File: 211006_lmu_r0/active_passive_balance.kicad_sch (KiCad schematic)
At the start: 37 parts, among them Q11 BSS308PE, T16 BUK9K13-60EX, T4 750312504

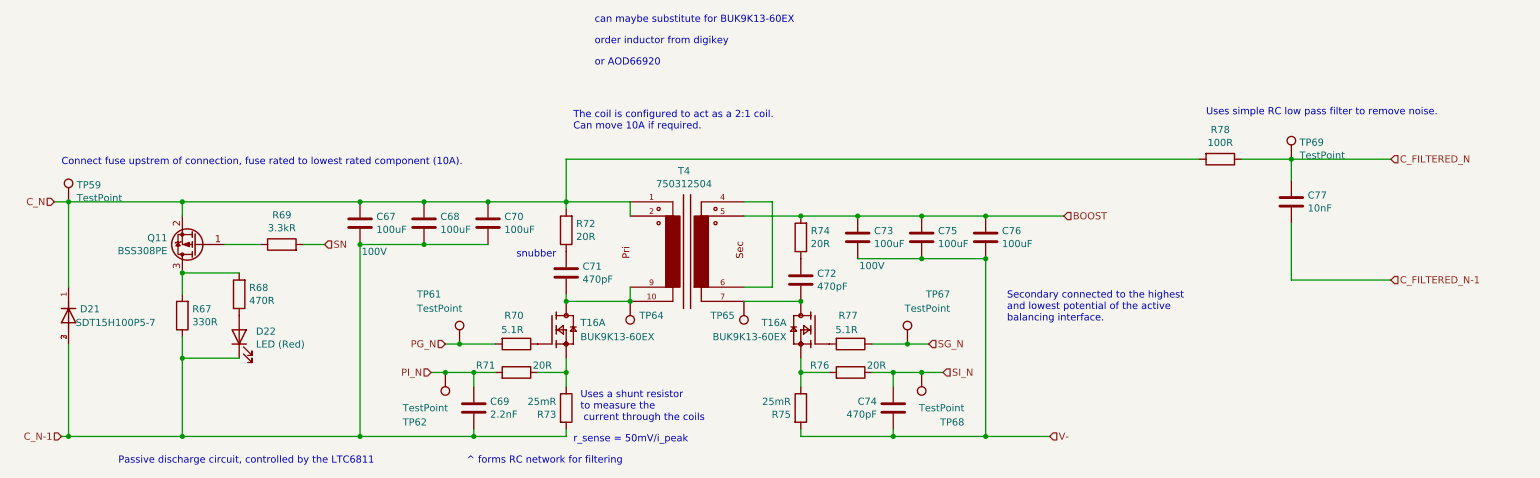
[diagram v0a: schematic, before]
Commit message: moved micro into position
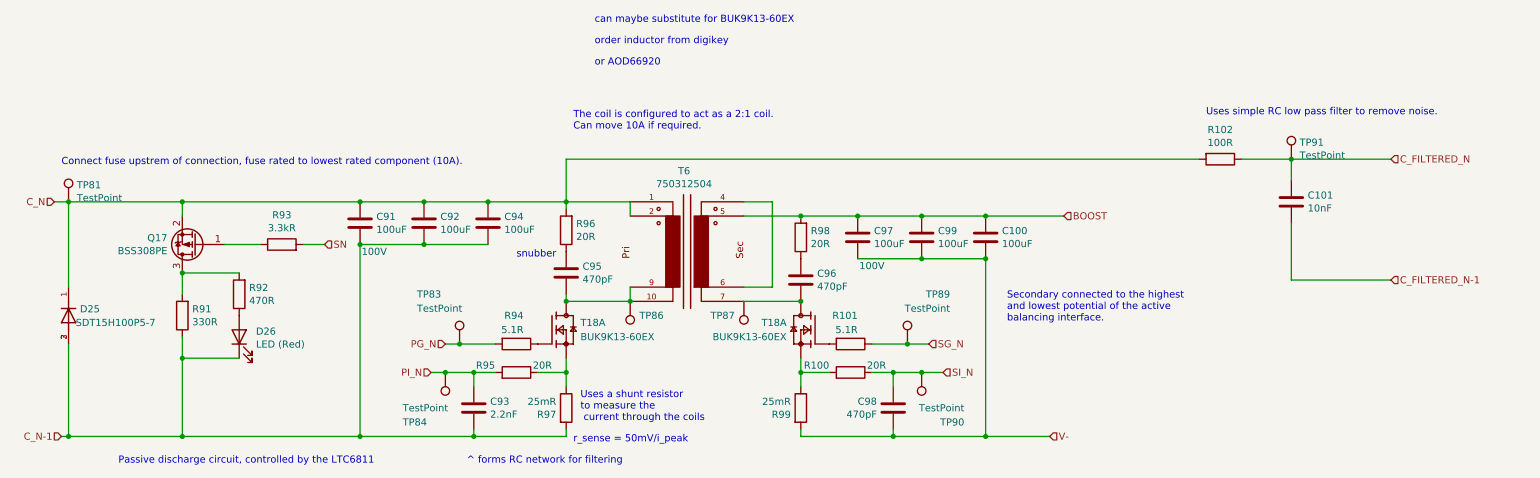
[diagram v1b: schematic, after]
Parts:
- renumbered C76 to C100, C77 to C101, C67 to C91, C68 to C92, C69 to C93, C70 to C94, C71 to C95, C72 to C96, C73 to C97, C74 to C98, C75 to C99, D21 to D25, D22 to D26, Q11 to Q17, R76 to R100, R77 to R101, R78 to R102, R67 to R91, R68 to R92, R69 to R93, R70 to R94, R71 to R95, R72 to R96, R73 to R97, R74 to R98, R75 to R99, T16 to T18, T4 to T6, TP59 to TP81, TP61 to TP83, TP62 to TP84, TP64 to TP86, TP65 to TP87, TP67 to TP89, TP68 to TP90, TP69 to TP91

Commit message: Routed vehicle section
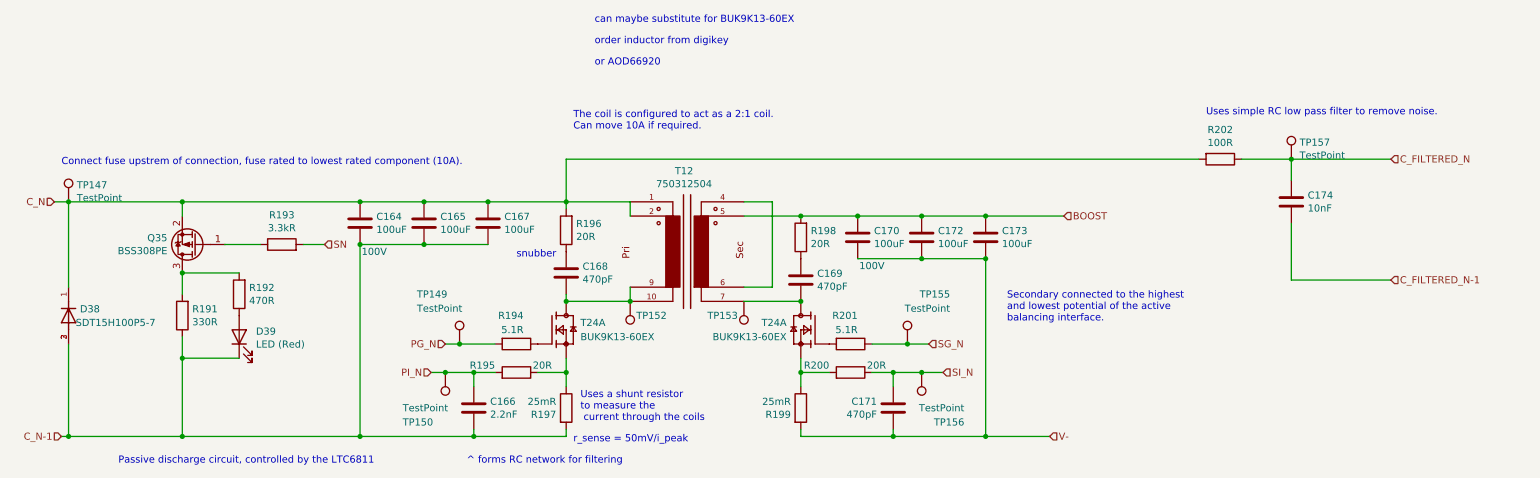
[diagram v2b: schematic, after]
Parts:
- renumbered C91 to C164, C92 to C165, C93 to C166, C94 to C167, C95 to C168, C96 to C169, C97 to C170, C98 to C171, C99 to C172, C100 to C173, C101 to C174, D25 to D38, D26 to D39, Q17 to Q35, R91 to R191, R92 to R192, R93 to R193, R94 to R194, R95 to R195, R96 to R196, R97 to R197, R98 to R198, R99 to R199, R100 to R200, R101 to R201, R102 to R202, T6 to T12, T18 to T24, TP81 to TP147, TP83 to TP149, TP84 to TP150, TP86 to TP152, TP87 to TP153, TP89 to TP155, TP90 to TP156, TP91 to TP157

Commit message: finished routing - beginning cleanup and review phase
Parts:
- renumbered C164 to C140, C165 to C141, C166 to C142, C167 to C143, C168 to C144, C169 to C145, C170 to C146, C171 to C147, C172 to C148, C173 to C149, C174 to C150, D38 to D34, D39 to D35, Q35 to Q29, R191 to R167, R192 to R168, R193 to R169, R194 to R170, R195 to R171, R196 to R172, R197 to R173, R198 to R174, R199 to R175, R200 to R176, R201 to R177, R202 to R178, T12 to T10, T24 to T22, TP147 to TP125, TP149 to TP127, TP150 to TP128, TP152 to TP130, TP153 to TP131, TP155 to TP133, TP156 to TP134, TP157 to TP135

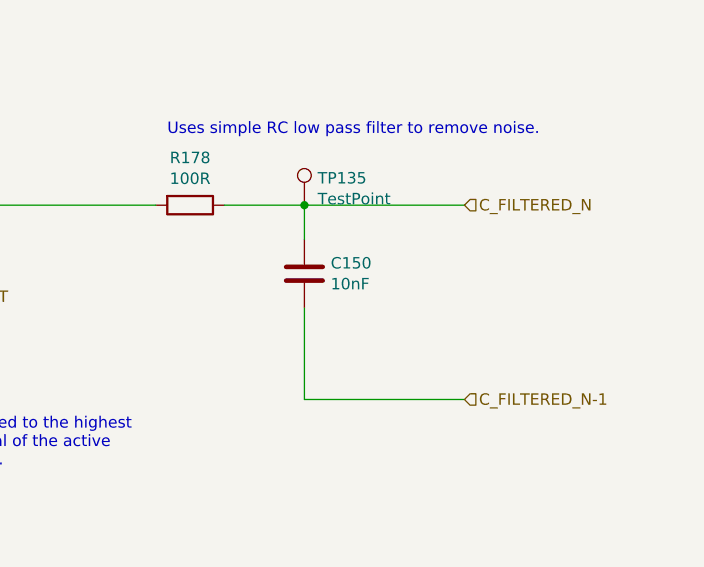
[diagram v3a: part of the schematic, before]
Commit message: silkscreen changes, shifting bun leds
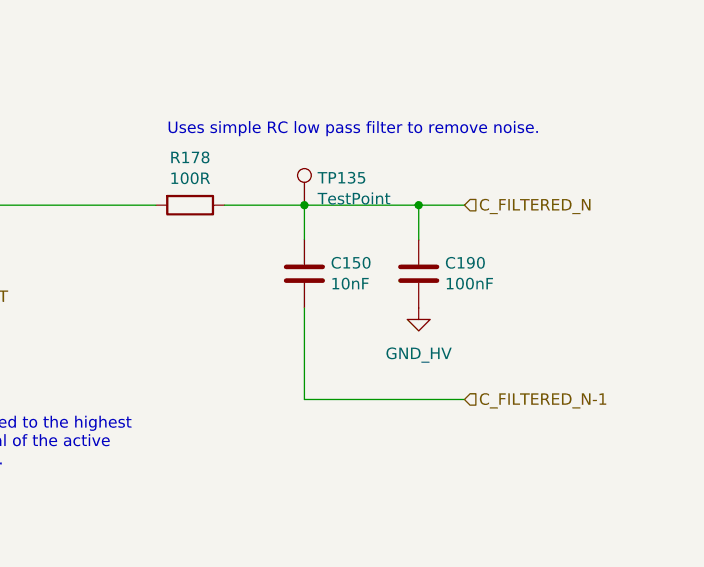
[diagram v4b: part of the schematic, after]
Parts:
- added C190: 100nF, Capacitor_SMD:C_1206_3216Metric_Pad1.33x1.80mm_HandSolder, symbol Device:C
- TP125, TP127, TP128, TP130, TP131, TP133, TP134, TP135: footprint TestPoint:TestPoint_Pad_D1.0mm -> custom:TestPoint_Pad_D1.0mm
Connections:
- net C_FILTERED_N: now also C190.2
- new net GND_HV: C190.1
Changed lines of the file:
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@@
   (junction (at 186.69 88.9) (diameter 0) (color 0 0 0 0)
   )
+  (junction (at 254 71.12) (diameter 0) (color 0 0 0 0)
+  )
   (junction (at 175.26 81.28) (diameter 0) (color 0 0 0 0)
   )
@@
     (stroke (width 0) (type default) (color 0 0 0 0))
   )
-  (wire (pts (xy 241.3 71.12) (xy 259.08 71.12))
+  (wire (pts (xy 241.3 71.12) (xy 254 71.12))
     (stroke (width 0) (type default) (color 0 0 0 0))
   )
@@
     (stroke (width 0) (type default) (color 0 0 0 0))
   )
+  (wire (pts (xy 254 71.12) (xy 259.08 71.12))
+    (stroke (width 0) (type default) (color 0 0 0 0))
+  )
   (wire (pts (xy 111.76 111.76) (xy 111.76 109.22))
     (stroke (width 0) (type default) (color 0 0 0 0))
@@
   )
   (wire (pts (xy 90.17 109.22) (xy 95.25 109.22))
+    (stroke (width 0) (type default) (color 0 0 0 0))
+  )
+  (wire (pts (xy 254 71.12) (xy 254 74.93))
     (stroke (width 0) (type default) (color 0 0 0 0))
   )
@@
       (effects (font (size 1.27 1.27)) (justify left))
     )
-    (property "Footprint" "TestPoint:TestPoint_Pad_D1.0mm" (id 2) (at 27.94 78.74 0)
+    (property "Footprint" "custom:TestPoint_Pad_D1.0mm" (id 2) (at 27.94 78.74 0)
       (effects (font (size 1.27 1.27)) hide)
     )
@@
       (effects (font (size 1.27 1.27)) (justify left))
     )
-    (property "Footprint" "TestPoint:TestPoint_Pad_D1.0mm" (id 2) (at 97.79 104.14 0)
+    (property "Footprint" "custom:TestPoint_Pad_D1.0mm" (id 2) (at 97.79 104.14 0)
       (effects (font (size 1.27 1.27)) hide)
     )
@@
       (effects (font (size 1.27 1.27)) (justify left))
     )
-    (property "Footprint" "TestPoint:TestPoint_Pad_D1.0mm" (id 2) (at 167.64 104.14 0)
+    (property "Footprint" "custom:TestPoint_Pad_D1.0mm" (id 2) (at 167.64 104.14 0)
       (effects (font (size 1.27 1.27)) hide)
     )
@@
       (effects (font (size 1.27 1.27)) (justify left))
     )
-    (property "Footprint" "TestPoint:TestPoint_Pad_D1.0mm" (id 2) (at 95.25 109.22 0)
+    (property "Footprint" "custom:TestPoint_Pad_D1.0mm" (id 2) (at 95.25 109.22 0)
       (effects (font (size 1.27 1.27)) hide)
     )
@@
       (effects (font (size 1.27 1.27)) (justify left))
     )
-    (property "Footprint" "TestPoint:TestPoint_Pad_D1.0mm" (id 2) (at 170.18 109.22 0)
+    (property "Footprint" "custom:TestPoint_Pad_D1.0mm" (id 2) (at 170.18 109.22 0)
       (effects (font (size 1.27 1.27)) hide)
     )
@@
       (effects (font (size 1.27 1.27)) (justify left))
     )
-    (property "Footprint" "TestPoint:TestPoint_Pad_D1.0mm" (id 2) (at 246.38 71.12 0)
+    (property "Footprint" "custom:TestPoint_Pad_D1.0mm" (id 2) (at 246.38 71.12 0)
       (effects (font (size 1.27 1.27)) hide)
     )
@@
       (effects (font (size 1.27 1.27)) hide)
     )
-    (property "Footprint" "TestPoint:TestPoint_Pad_D1.0mm" (id 2) (at 128.27 96.52 0)
+    (property "Footprint" "custom:TestPoint_Pad_D1.0mm" (id 2) (at 128.27 96.52 0)
       (effects (font (size 1.27 1.27)) hide)
     )
@@
       (effects (font (size 1.27 1.27)) hide)
     )
-    (property "Footprint" "TestPoint:TestPoint_Pad_D1.0mm" (id 2) (at 138.43 96.52 0)
+    (property "Footprint" "custom:TestPoint_Pad_D1.0mm" (id 2) (at 138.43 96.52 0)
       (effects (font (size 1.27 1.27)) hide)
     )
@@
     (pin "S1")
   )
+  (symbol (lib_id "Device:C") (at 254 78.74 180)
+    (in_bom yes) (on_board yes)
+    (property "Reference" "C190" (id 0) (at 256.921 77.5716 0)
+      (effects (font (size 1.27 1.27)) (justify right))
+    )
+    (property "Value" "100nF" (id 1) (at 256.921 79.883 0)
+      (effects (font (size 1.27 1.27)) (justify right))
+    )
+    (property "Footprint" "Capacitor_SMD:C_1206_3216Metric_Pad1.33x1.80mm_HandSolder" (id 2) (at 253.0348 74.93 0)
+      (effects (font (size 1.27 1.27)) hide)
+    )
+    (property "Datasheet" "~" (id 3) (at 254 78.74 0)
+      (effects (font (size 1.27 1.27)) hide)
+    )
+    (property "Part Number" "-" (id 4) (at 254 78.74 0)
+      (effects (font (size 1.27 1.27)) hide)
+    )
+    (property "Manufacturer" "-" (id 5) (at 254 78.74 0)
+      (effects (font (size 1.27 1.27)) hide)
+    )
+    (pin "1")
+    (pin "2")
+  )
   (symbol (lib_id "BUK9K17-60E:BUK9K17-60E") (at 156.21 101.6 0) (mirror y)
     (in_bom yes) (on_board yes) (fields_autoplaced)
@@
     (pin "S2")
   )
+  (symbol (lib_id "gnd_hv:GND_HV") (at 254 82.55 0)
+    (in_bom yes) (on_board yes) (fields_autoplaced)
+    (property "Reference" "#PWR0117" (id 0) (at 254 88.9 0)
+      (effects (font (size 1.27 1.27)) hide)
+    )
+    (property "Value" "GND_HV" (id 1) (at 254 87.63 0))
+    (property "Footprint" "" (id 2) (at 254 82.55 0)
+      (effects (font (size 1.27 1.27)) hide)
+    )
+    (property "Datasheet" "" (id 3) (at 254 82.55 0)
+      (effects (font (size 1.27 1.27)) hide)
+    )
+    (pin "1")
+  )
 )

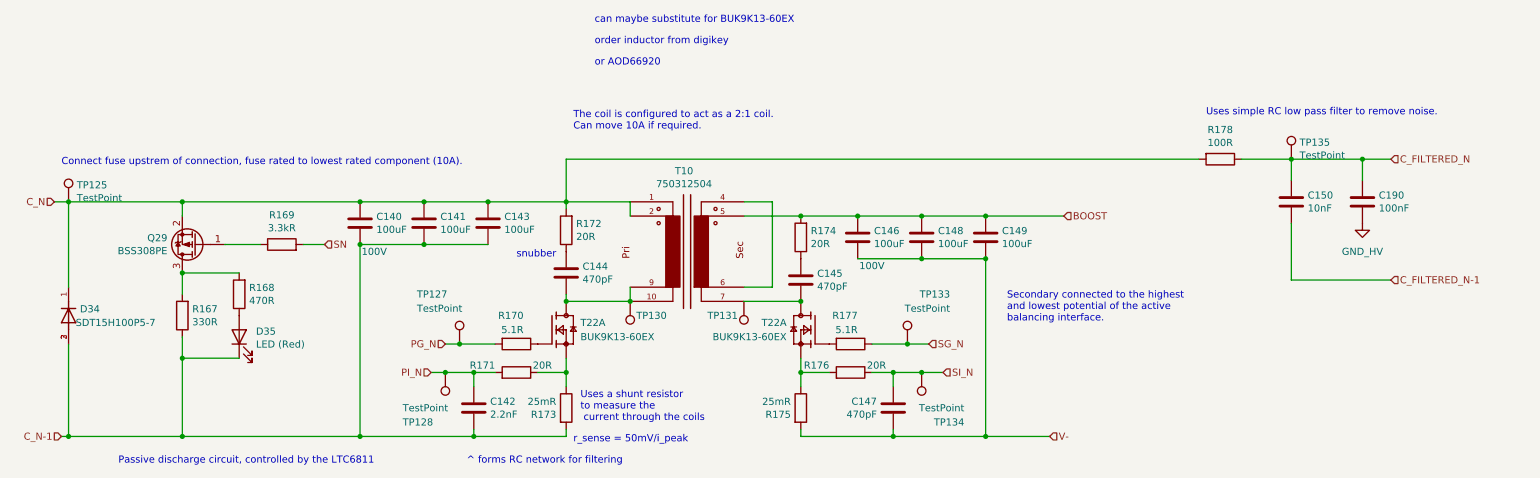
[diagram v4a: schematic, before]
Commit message: going to bulk edit fields
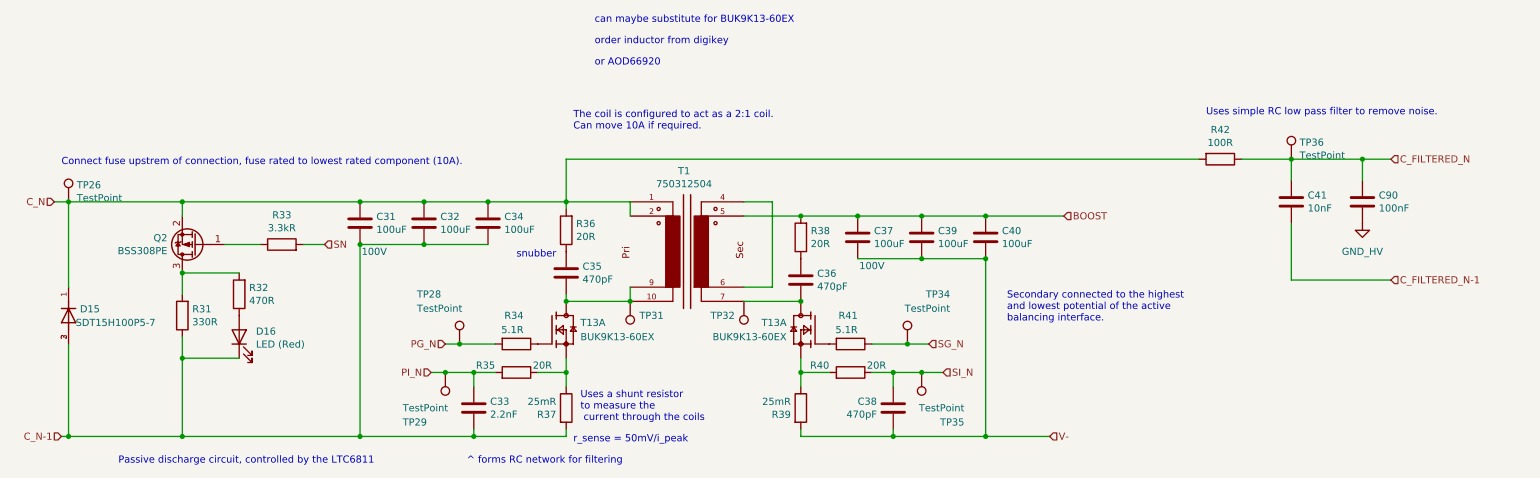
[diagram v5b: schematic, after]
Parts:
- renumbered C140 to C31, C141 to C32, C142 to C33, C143 to C34, C144 to C35, C145 to C36, C146 to C37, C147 to C38, C148 to C39, C149 to C40, C150 to C41, C190 to C90, D34 to D15, D35 to D16, Q29 to Q2, R167 to R31, R168 to R32, R169 to R33, R170 to R34, R171 to R35, R172 to R36, R173 to R37, R174 to R38, R175 to R39, R176 to R40, R177 to R41, R178 to R42, T10 to T1, T22 to T13, TP125 to TP26, TP127 to TP28, TP128 to TP29, TP130 to TP31, TP131 to TP32, TP133 to TP34, TP134 to TP35, TP135 to TP36
